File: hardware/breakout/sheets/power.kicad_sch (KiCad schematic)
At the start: 41 parts, among them J1 MiniDIN_4, U1 TPS7A4901, U2 LD1117S33TR_SOT223, U3 IH1215D, U4 TPS7A4901, U5 TPS7A3001

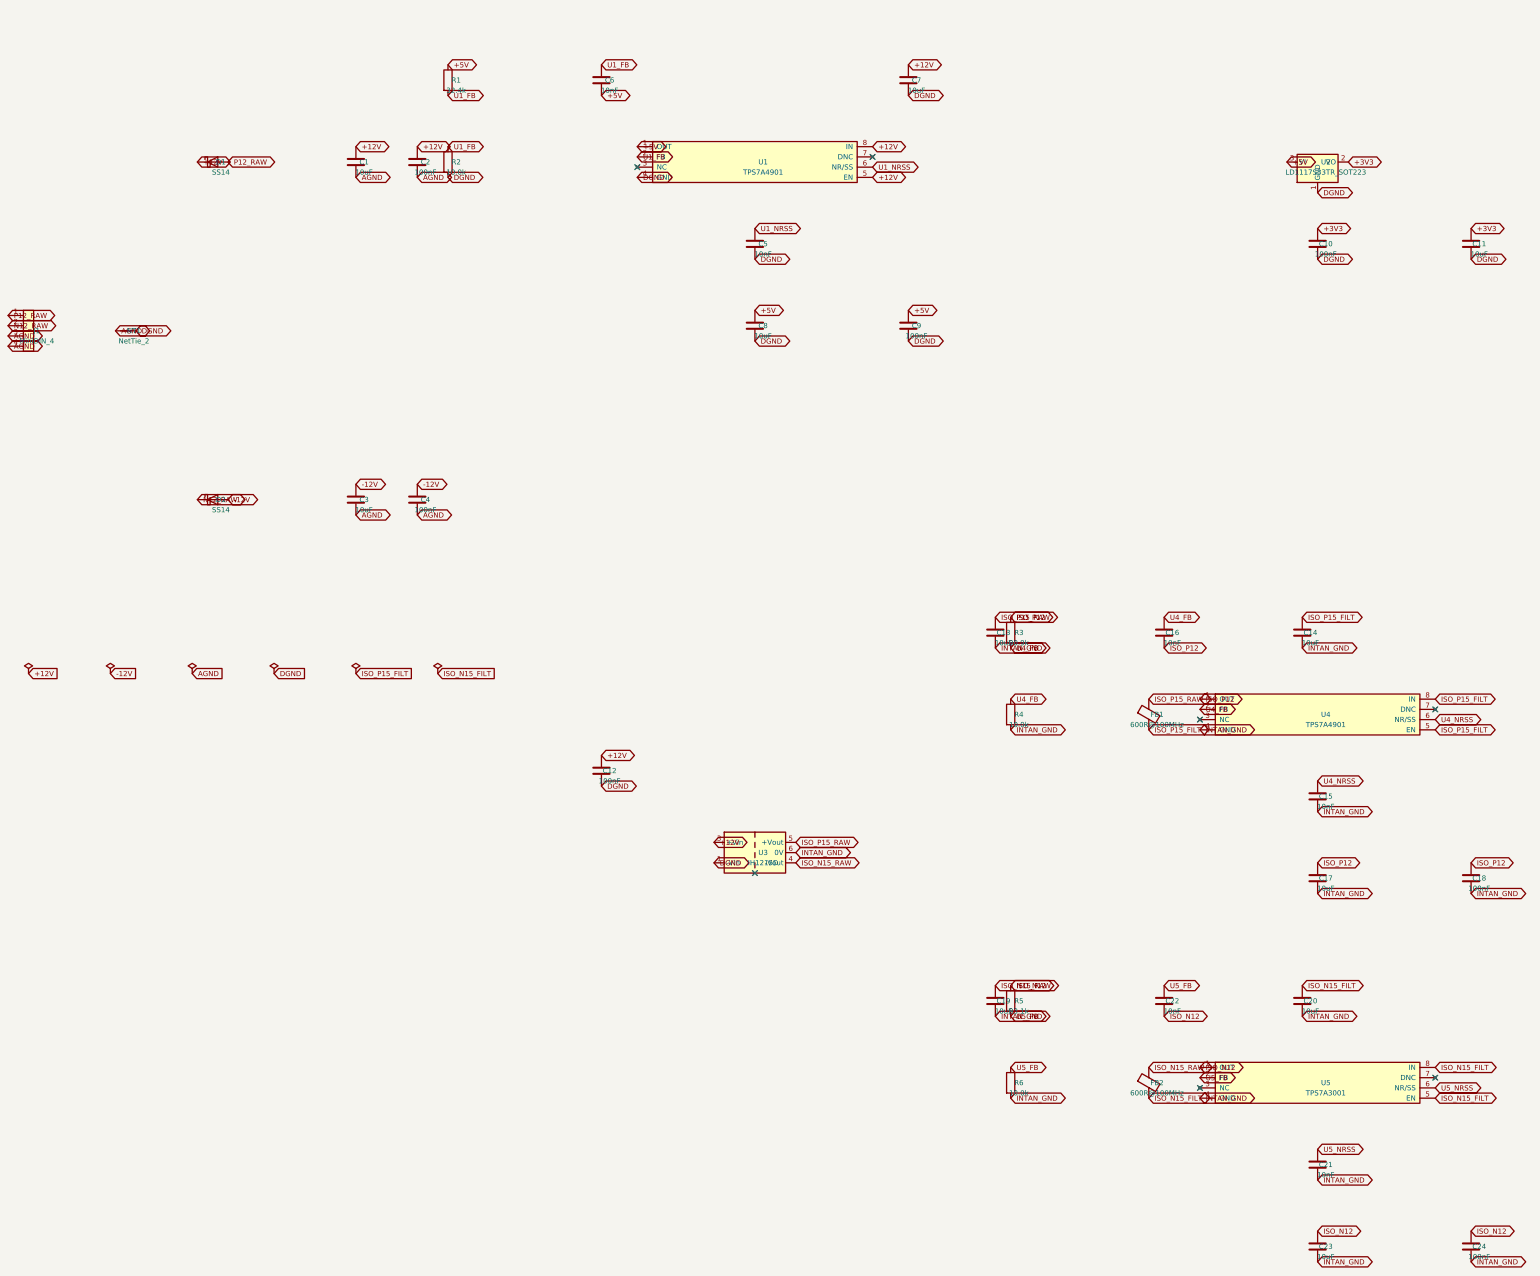
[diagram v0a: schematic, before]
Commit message: fix(hw): +5V direct from inlet not +12V regulator, real instance-path ancestry
Coordinator review, fix round 1. Two findings against the power sheet.

Finding 1 -- the +5V rail was undersized by roughly a factor of two. Worst
case ~26 simultaneous optocoupler LEDs draw ~180-260mA against TPS7A4901's
150mA cap, before counting the 74HCT541 buffers on the same rail. A bigger
linear regulator dissipates ~1.9W in a sealed 2U chassis already carrying
10-15W; a switcher would contradict this design's own switcher-count-of-one
decision. Fix: +5V now comes directly off a fifth inlet pin instead of being
regulated down from +12V on board.

  - Inlet widened 4-pin -> 5-pin mini-DIN (new MiniDIN_5 symbol/footprint,
    Same Sky MD-50SN -- same primary datasheet as MiniDIN_4, confirmed panel
    envelope/bushing/mounting-ear dimensions are shared across the whole
    MD-30SN..MD-80SN family, not assumed). D3 (SS14) protects the new rail,
    same orientation as D1 (both "positive" outputs of the same supply).
    Entry bulk/bypass on +5V reference DGND, not AGND like its neighbours --
    +5V is DGND-referenced for its whole life on this sheet, so its entry
    caps are too, deliberately asymmetric with +12V/-12V's own AGND caps.
    Budgeted for 400mA.
  - TPS7A4901-for-+5V stage removed entirely (regulator, FB divider, CIN/
    COUT). LD1117 (+3V3) now sources from +5V, not +12V: ~5x less
    dissipation than +12V at the same load, still clears LD1117's dropout
    spec with margin at the light currents digital logic draws. Documented,
    not silently decided.
  - References renumbered against the real regenerated netlist (U2->U1,
    U3->U2, U4->U3, U5->U4); internal coordinate/variable names in
    gen_breakout_power.py kept in sync with the real output, not left stale.

Finding 2 -- the child sheet's own component `(instances (path ...))`
ancestor chain was self-referential (power.kicad_sch's own root uuid)
instead of the real breakout-root + "power"-sheet-symbol chain a 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
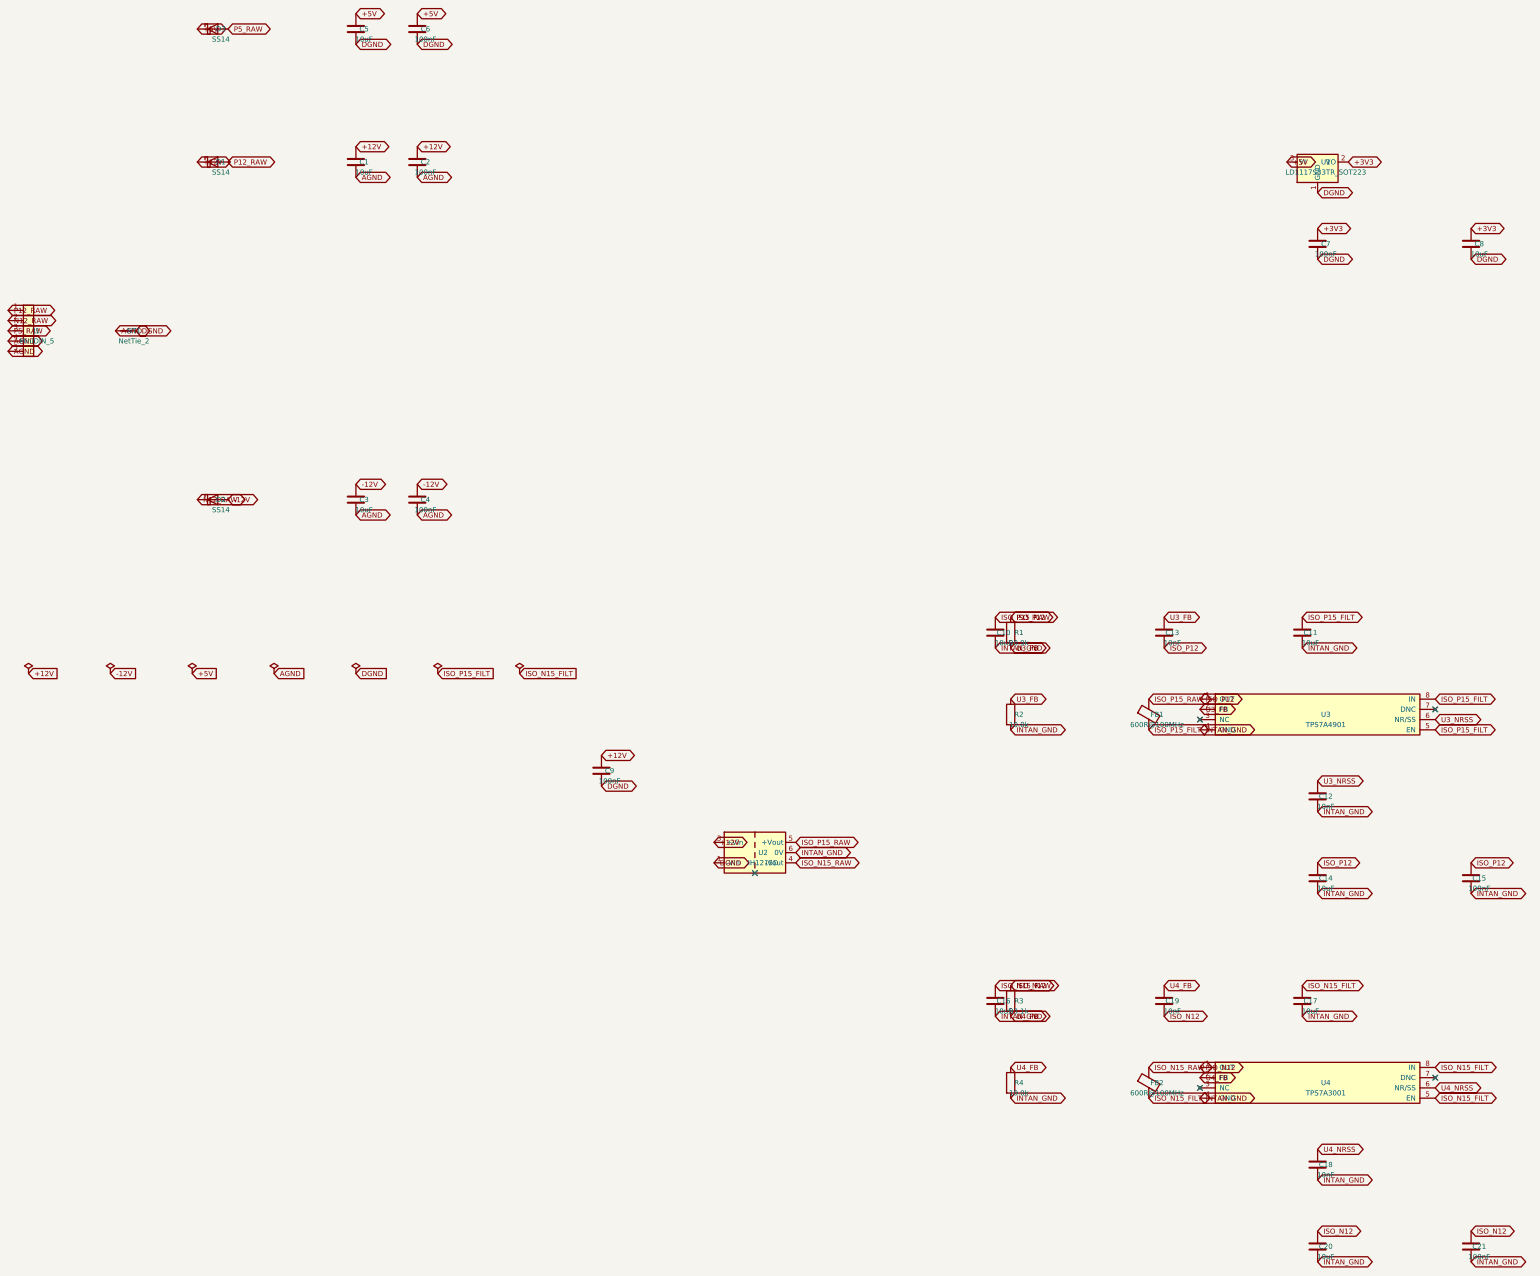
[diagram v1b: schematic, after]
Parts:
- removed C22: 10nF, Capacitor_SMD:C_0603_1608Metric, symbol Device:C
- removed C23: 10uF, Capacitor_SMD:C_0805_2012Metric, symbol Device:C
- removed C24: 100nF, Capacitor_SMD:C_0603_1608Metric, symbol Device:C
- removed J1: MiniDIN_4, wl-sync:MiniDIN_4_Panel, symbol wl-sync:MiniDIN_4
- removed R5: 93.1k, Resistor_SMD:R_0603_1608Metric, symbol Device:R
- removed R6: 10.0k, Resistor_SMD:R_0603_1608Metric, symbol Device:R
- removed U1, U4: TPS7A4901, Package_SO:HVSSOP-8-1EP_3x3mm_P0.65mm_EP1.57x1.89mm, symbol wl-sync:TPS7A4901
- removed U2: LD1117S33TR_SOT223, Package_TO_SOT_SMD:SOT-223-3_TabPin2, symbol Regulator_Linear:LD1117S33TR_SOT223
- removed U3: IH1215D, Converter_DCDC:Converter_DCDC_XP_POWER-IHxxxxD_THT, symbol Converter_DCDC_Isolated:IH1215D
- removed U5: TPS7A3001, Package_SO:HVSSOP-8-1EP_3x3mm_P0.65mm_EP1.57x1.89mm, symbol wl-sync:TPS7A3001
- added D3: SS14, Diode_SMD:D_SMA_Handsoldering, symbol Diode:SS14
- added J1: MiniDIN_5, wl-sync:MiniDIN_5_Panel, symbol wl-sync:MiniDIN_5
- added U1: LD1117S33TR_SOT223, Package_TO_SOT_SMD:SOT-223-3_TabPin2, symbol Regulator_Linear:LD1117S33TR_SOT223
- added U2: IH1215D, Converter_DCDC:Converter_DCDC_XP_POWER-IHxxxxD_THT, symbol Converter_DCDC_Isolated:IH1215D
- added U3: TPS7A4901, Package_SO:HVSSOP-8-1EP_3x3mm_P0.65mm_EP1.57x1.89mm, symbol wl-sync:TPS7A4901
- added U4: TPS7A3001, Package_SO:HVSSOP-8-1EP_3x3mm_P0.65mm_EP1.57x1.89mm, symbol wl-sync:TPS7A3001
- C10: value 100nF -> 10uF; footprint Capacitor_SMD:C_0603_1608Metric -> Capacitor_SMD:C_0805_2012Metric
- C12, C18: value 100nF -> 10nF
- C13, C19: value 10uF -> 10nF; footprint Capacitor_SMD:C_0805_2012Metric -> Capacitor_SMD:C_0603_1608Metric
- C15, C21, C6: value 10nF -> 100nF
- C16, C5: value 10nF -> 10uF; footprint Capacitor_SMD:C_0603_1608Metric -> Capacitor_SMD:C_0805_2012Metric
- C7: value 10uF -> 100nF; footprint Capacitor_SMD:C_0805_2012Metric -> Capacitor_SMD:C_0603_1608Metric
- R1: value 32.4k -> 90.9k
- R3: value 90.9k -> 93.1k
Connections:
- net U1_NRSS is gone; now on net +5V: C5.1
- net U5_NRSS is gone; now on net ISO_N12: C21.1
- net +12V: now also C9.1, U2.3 (+Vin); no longer C12.1, C7.1
- net +3V3: now also C7.1, C8.1, U1.2 (VO); no longer C10.1, C11.1
- net +5V: now also C6.1, D3.1 (K), U1.3 (VI); no longer C6.2, C8.1, C9.1, R1.1
- net AGND: now also J1.4, J1.5
- net DGND: now also C6.2, U1.1 (GND), U2.1 (-Vin); no longer C10.2, C11.2, C12.2, R2.2
- net INTAN_GND: now also C10.2, C11.2, C12.2, C16.2, R2.2, U2.6 (0V), U3.4 (GND), U4.4 (GND); no longer C13.2, C19.2
- net ISO_N12: now also C19.2, C20.1, R3.1, U4.1 (OUT)
- net ISO_N15_FILT: now also C17.1, U4.5 (EN), U4.8 (IN); no longer C20.1
- net ISO_N15_RAW: now also C16.1, U2.4 (-Vout); no longer C19.1
- net ISO_P12: now also C13.2, C14.1, C15.1, R1.1, U3.1 (OUT); no longer C16.2, C17.1, C18.1, R3.1
- net ISO_P15_FILT: now also C11.1, U3.5 (EN), U3.8 (IN); no longer C14.1
- net ISO_P15_RAW: now also C10.1, U2.5 (+Vout); no longer C13.1
- net N12_RAW: now also J1.2
- net P12_RAW: now also J1.1
- net U4_FB: now also C19.1, U4.2 (FB); no longer C16.1
- net U4_NRSS: now also C18.1, U4.6 (NR/SS); no longer C15.1
- net U1_FB renamed U3_FB
- net U3_FB: now also C13.1, U3.2 (FB); no longer C6.1
- new net P5_RAW: D3.2 (A), J1.3
- new net U3_NRSS: C12.1, U3.6 (NR/SS)
- no-connect marks 7 -> 5

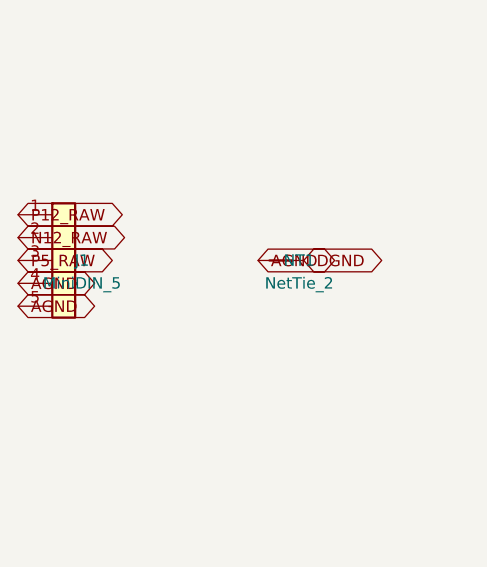
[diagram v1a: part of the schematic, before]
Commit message: fix(hw): replace mini-DIN power inlet with keyed, locking M12 connector
Coordinator review, fix round 2. The power sheet's electrical design passed
review clean; this finding is about one connector's footprint.

build_minidin() drew both MiniDIN_4_Panel and MiniDIN_5_Panel on an evenly
spaced ring. The reviewer pulled Same Sky's own MD-SN datasheet and
confirmed the per-pin-count diagrams for both MD-40SN and MD-50SN show a
clustered layout instead -- a topology error, not a tolerance one, that as
fabbed would very likely have failed to mate. Redrawing against MD-SN
wasn't an option regardless: both parts are discontinued (rev 1.06/1.07,
2022/2023, verified against the manufacturer PDF).

Replaced with Amphenol LTW M12A-05PFFP-SF8001, selected against the
review's own priority order and checked, not assumed, against each:
current production, ACTIVE lifecycle status with real stock at DigiKey
(811 units) and Mouser (1,081 units); a real 2D/3D drawing is publicly
downloadable from the manufacturer's own product page and DigiKey's EDA
tab; 5 positions carrying +12V/-12V/+5V/GND/shield; IEC 61076-2-101
A-coded, so the shell cannot mate rotated; M12x1 threaded coupling, a true
lock for a chassis that slides in and out of a rack; front-fastened panel
mount with PCB solder pins, consistent with every other connector on this
board; a shell diameter comparable to the mini-DIN bushing it replaces.

Contact geometry (four contacts on a 5.0mm pitch circle at 90 degree
spacing, 45 degrees off the keyway, one at dead centre) is the IEC
61076-2-101 A-coding standard geometry -- confirmed against the standard
document itself and cross-checked against a different manufacturer's own
current M12 datasheet, not modelled as a guess. Two dimensions (panel
cutout, external shell reference) could not be pulled from Amphenol LTW's
own drawing specifically -- a real drawing exists but its download is
JS-gated -- and are flagged in hardware/README.md's confidence table for
verification before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
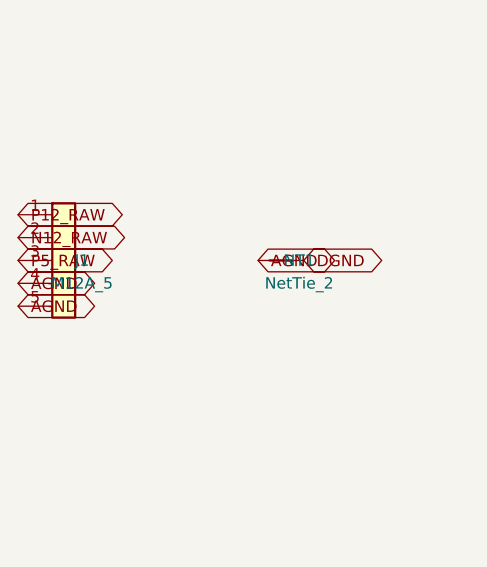
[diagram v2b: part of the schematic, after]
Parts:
- removed J1: MiniDIN_5, wl-sync:MiniDIN_5_Panel, symbol wl-sync:MiniDIN_5
- added J1: M12A_5, wl-sync:M12A_5_Panel, symbol wl-sync:M12A_5
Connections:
- net AGND: now also J1.4, J1.5
- net N12_RAW: now also J1.2
- net P12_RAW: now also J1.1
- net P5_RAW: now also J1.3

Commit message: feat(hw): fan headers on the power sheet -- dedicated FAN_12V/FAN_RTN, polyfused
Spec Sec.9.5 recorded the thermal requirement and the four 3-pin fan-header
connectors it needed, but the schematic never actually placed them.

Four Connector_Generic:Conn_01x03 headers at 2.54mm, standard PC fan pinout
(pin 1 GND, pin 2 +12V, pin 3 tach). Tach is a deliberate no-connect --
power-only was chosen because the sync module's GPIO is full at 26 of 28 --
with an on-sheet note so the third pin doesn't get "tidied up" later.

Fan current gets its own FAN_12V/FAN_RTN nets rather than riding AGND/DGND:
a brushless DC fan is a commutating switching load, and running ~240mA of
it through the analog ground would contradict this design's own rejection
of digital isolators for an RF carrier (spec Sec.2 decision 3) and of
on-board switchers for consistency (spec Sec.8). FAN_RTN joins DGND (not
AGND -- mirroring where the isolated DC-DC's primary side and +5V's own
entry caps already put their own noise) at exactly one point via a second
NetTie_2, so ERC keeps treating it as a distinct net everywhere else.
FAN_12V derives from the already-protected +12V through a new polyfuse,
Littelfuse 1206L050/15YR (500mA hold / 1A trip / 15V max, 34k+ in stock at
DigiKey): ~2.1x margin over the 240mA nominal four-fan load, sized for PPTC
ambient derating in a sealed, thermally-loaded chassis and fan inrush at
power-up, not just the bare steady-state figure. Local 10uF+100nF bulk
capacitance sits on FAN_12V after the fuse, referenced to FAN_RTN.

New references (J52-J55, F1, C147-C148, NT2, #PWR9-10) are minted
out-of-band past the whole board's real committed maxima -- power.kicad_sch
is the first sheet this project ever generated, so every sibling sheet
already seeded its own numbering past this file's pre-fan-header state.
Confirmed by a semantic ref/value/footprint diff against git HEAD across
all ten sheets: 10 additions, 0 renumbered, 0 removed, no other sheet
touched.

check_breakout_power_ne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
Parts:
- added C147: 10uF, Capacitor_SMD:C_0805_2012Metric, symbol Device:C
- added C148: 100nF, Capacitor_SMD:C_0603_1608Metric, symbol Device:C
- added F1: 1206L050/15YR, Fuse:Fuse_1206_3216Metric_Pad1.42x1.75mm_HandSolder, symbol Device:Polyfuse
- added J52: Chassis fan 1, Connector_PinHeader_2.54mm:PinHeader_1x03_P2.54mm_Vertical, symbol Connector_Generic:Conn_01x03
- added J53: Chassis fan 2, Connector_PinHeader_2.54mm:PinHeader_1x03_P2.54mm_Vertical, symbol Connector_Generic:Conn_01x03
- added J54: Chassis fan 3, Connector_PinHeader_2.54mm:PinHeader_1x03_P2.54mm_Vertical, symbol Connector_Generic:Conn_01x03
- added J55: Chassis fan 4, Connector_PinHeader_2.54mm:PinHeader_1x03_P2.54mm_Vertical, symbol Connector_Generic:Conn_01x03
- added NT2: NetTie_2, NetTie:NetTie-2_SMD_Pad2.0mm, symbol Device:NetTie_2
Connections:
- net +12V: now also F1.1
- net DGND: now also NT2.2
- new net FAN_12V: C147.1, C148.1, F1.2, J52.2 (Pin_2), J53.2 (Pin_2), J54.2 (Pin_2), J55.2 (Pin_2)
- new net FAN_RTN: C147.2, C148.2, J52.1 (Pin_1), J53.1 (Pin_1), J54.1 (Pin_1), J55.1 (Pin_1), NT2.1
- no-connect marks 5 -> 9
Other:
- note added: "+12V through F1 (polyfuse, 1206L050/15YR: 500mA hold / 1A trip) so a stalled"
- note added: "3) and on-board switchers for consistency (spec Sec.8). FAN_12V derives from"
- note added: "FAN_12V/FAN_RTN are dedicated nets, never AGND/DGND directly: a fan is a"
- note added: "FAN_RTN joins DGND at exactly one point (NT2), mirroring how AGND/DGND join"
- note added: "Four chassis fan headers (spec Sec.9.5, added 2026-08-15): standard PC 3-pin"
- note added: "NT1, never by a direct shared pin."
- note added: "PIN 3 (TACH) IS A DELIBERATE NO-CONNECT -- DO NOT DELETE THE PIN. Power-only"
- note added: "adding tach later a wire change, not a connector change."
- note added: "at J1 -- so FAN_RTN reaches AGND too, but only transitively, through NT2 then"
- note added: "commutating switching load, and its ~240mA through the analog ground would"
- note added: "contradict rejecting digital isolators for an RF carrier (spec Sec.2 decision"
- note added: "fan pinout, 2.54mm -- pin 1 GND, pin 2 +12V, pin 3 tach."
- note added: "or shorted fan cannot pull down the rails the analog section depends on."
- note added: "third pin lets a 3- or 4-pin Noctua-class plug seat with no adapter, and makes"
- note added: "was chosen because the sync module's GPIO is full at 26 of 28; keeping the"
